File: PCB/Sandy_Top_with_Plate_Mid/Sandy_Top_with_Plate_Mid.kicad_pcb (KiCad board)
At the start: 2 copper layers, 285 x 75.1 mm, 63 parts, among them J1 Conn_02x02_Top_Bottom, J2 Conn_02x02_Top_Bottom, J3 Conn_02x02_Top_Bottom

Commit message: ネジ穴調整、追加
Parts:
- removed D15: D, locallib:D_SOD-123_Emphasized_Direction_Line
- removed EXT_TC7: Conn_01x01, TestPoint:TestPoint_THTPad_D2.0mm_Drill1.0mm
- removed the SW_=1 at (291.3, 27.0)
- added H10: MountingHole, locallib:MountingHole_2.2mm_M2_Pad_minimal, F.Cu at (291.3, 52.0)
- added H11: MountingHole, locallib:MountingHole_2.2mm_M2_Pad_minimal, F.Cu at (138.9, 74.1)
- added H12: MountingHole, locallib:MountingHole_2.2mm_M2_Pad_minimal, F.Cu at (177.0, 74.1)
- added H9: MountingHole, locallib:MountingHole_2.2mm_M2_Pad_minimal, F.Cu at (253.2, 28.2)
- REF**: footprint locallib:60_Outline-Sandy-Top3-with-Mid-plate-from-Mid4 -> locallib:60_Outline-Sandy-DN0040-Top
- moved H6 219.1 mm to (62.7, 28.2), turned to 180 degrees
- moved H5 201.4 mm to (24.6, 52.0)
- moved H4 200.2 mm to (291.3, 20.6), turned to 180 degrees
- moved H3 162.1 mm to (196.1, 20.6), turned to 180 degrees
- moved H1 104.8 mm to (24.6, 20.6)
- moved H2 66.7 mm to (119.9, 20.6)
- moved D9 28.6 mm to (186.6, 30.6)
- moved SW_6 28.6 mm to (186.6, 27.0)
- moved D8 28.6 mm to (167.5, 30.6)
- moved SW_=1 28.6 mm to (167.5, 27.0)
- moved D7 28.6 mm to (148.5, 30.6)
- moved SW_-1 28.6 mm to (148.5, 27.0)
- moved H8 19.1 mm to (196.1, 52.0)
- moved H7 19.0 mm to (119.9, 52.0)
- moved D14 9.53 mm to (281.8, 30.6)
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- renumbered SW_6 to SW_-1, SW_\1 to SW_6, SW_`1 to SW_=1, SW_-1 to SW_INS1
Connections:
- H1 pad 1: Top_GND -> unconnected-(H1-Pad1)
- H2 pad 1: Top_GND -> unconnected-(H2-Pad1)
- H3 pad 1: Top_GND -> unconnected-(H3-Pad1)
- H4 pad 1: Top_GND -> unconnected-(H4-Pad1)
- H5 pad 1: Top_GND -> unconnected-(H5-Pad1)
- H6 pad 1: Top_GND -> unconnected-(H6-Pad1)
- H7 pad 1: Top_GND -> unconnected-(H7-Pad1)
- H8 pad 1: Top_GND -> unconnected-(H8-Pad1)
- J1 pad 4: Top_col7 -> unconnected-(J1-Pin_4-Pad4)_1
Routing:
- net Top_row0: track 286.8 -> 0.00 mm, vias 2 -> 0
- net Top_row5: track 250.6 -> 0.00 mm, vias 2 -> 0
- net Top_col7: track 134.7 -> 0.00 mm, vias 2 -> 0
- net Top_col0: track 125.2 -> 0.00 mm, vias 2 -> 0
- net Top_col6: track 110.4 -> 0.00 mm, vias 2 -> 0
- net Top_col3: track 99.5 -> 0.00 mm, vias 1 -> 0
- net Top_col1: track 91.6 -> 0.00 mm, vias 3 -> 0
- net Top_col2: track 79.6 -> 0.00 mm, vias 5 -> 0
- net Top_col5: track 73.4 -> 0.00 mm, vias 3 -> 0
- net Top_row1: track 66.0 -> 0.00 mm, vias 1 -> 0
- net Top_row6: track 65.9 -> 0.00 mm, vias 1 -> 0
- net Top_col4: track 65.7 -> 0.00 mm, vias 3 -> 0
- net Net-(D3-A): track 10.7 -> 0.00 mm
- net Net-(D8-A): track 10.4 -> 0.00 mm
- net Net-(D7-A): track 10.4 -> 0.00 mm
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- added copper zone on B.Cu, net unconnected-(H5-Pad1)
- added copper zone on F.Cu, net unconnected-(H5-Pad1)
- removed copper zone on B.Cu, net Top_GND
- removed copper zone on F.Cu, net Top_GND
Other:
- outline, holes or cut-outs redrawn
- board text added: "Screw to Bottom ↓"
- board text removed: "SW_6, `, \ の3個の並び順が間違っているが、 v01とのソフト的な互換性を保つため、修正はおこなわない。"

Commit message: 基板間ピン割り当て
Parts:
- moved EXT_TR1 29.9 mm to (119.9, 34.1), turned to 0 degrees
- moved EXT_TR6 26.2 mm to (119.9, 37.7)
- moved EXT_TR5 14.5 mm to (24.6, 34.1)
- moved EXT_TC1 9.53 mm to (81.8, 21.1)
- moved EXT_TC3 9.53 mm to (158.0, 21.1)
- moved EXT_TC5 9.53 mm to (234.2, 21.1)
- moved J2 9.53 mm to (158.0, 29.6)
- moved EXT_TC0 9.52 mm to (43.7, 21.1)
- moved EXT_TC2 9.52 mm to (100.8, 21.1)
- moved EXT_TC4 9.52 mm to (177.0, 21.0)
- moved EXT_TC6 9.52 mm to (272.3, 21.1)
- moved J1 9.52 mm to (177.0, 29.6)
- moved EXT_TR0 4.91 mm to (24.6, 30.6)
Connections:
- H1 pad 1: unconnected-(H1-Pad1) -> Top_col0
- H10 pad 1: unconnected-(H10-Pad1) -> Top_row5
- H11 pad 1: unconnected-(H11-Pad1) -> Top_row1
- H12 pad 1: unconnected-(H12-Pad1) -> Top_row6
- H2 pad 1: unconnected-(H2-Pad1) -> Top_col2
- H3 pad 1: unconnected-(H3-Pad1) -> Top_col4
- H4 pad 1: unconnected-(H4-Pad1) -> Top_col6
- H5 pad 1: unconnected-(H5-Pad1) -> Top_row0
- H6 pad 1: unconnected-(H6-Pad1) -> Top_col1
- H7 pad 1: unconnected-(H7-Pad1) -> Top_col3
- H8 pad 1: unconnected-(H8-Pad1) -> Top_GND
- H9 pad 1: unconnected-(H9-Pad1) -> Top_col5
- J1 pad 4: unconnected-(J1-Pin_4-Pad4)_1 -> Top_GND
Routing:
- net Top_col0: track 0.00 -> 29.2 mm
- added copper zone on B.Cu, net Top_row0
- added copper zone on F.Cu, net Top_row0
- removed copper zone on B.Cu, net unconnected-(H5-Pad1)
- removed copper zone on F.Cu, net unconnected-(H5-Pad1)

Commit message: ネジ穴と接続するピンを調整中
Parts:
- added D15: D, locallib:D_SOD-123_Emphasized_Direction_Line, B.Cu at (148.3, 68.7)
- added D20: D, locallib:D_SOD-123_Emphasized_Direction_Line, B.Cu at (167.5, 68.7)
- added EXT_TR2: Conn_01x01, TestPoint:TestPoint_THTPad_D2.0mm_Drill1.0mm, B.Cu at (142.5, 56.8)
- added H13: MountingHole, locallib:MountingHole_2.2mm_M2_Pad_minimal, F.Cu at (158.0, 74.1)
- added SW_'1: SW_Push, MX_Alps_Hybrid:MXOnly-1U-Hotswap-guide, F.Cu at (167.5, 65.1)
- added SW_;1: SW_Push, MX_Alps_Hybrid:MXOnly-1U-Hotswap-guide, F.Cu at (148.5, 65.1)
- moved H7 30.5 mm to (215.1, 28.2), turned to 180 degrees
- moved H6 30.5 mm to (100.8, 28.2), turned to 180 degrees
- moved H9 29.2 mm to (196.1, 52.0)
- moved H12 29.2 mm to (119.9, 52.0)
- moved EXT_TR1 27.4 mm to (142.5, 49.6)
- moved EXT_TR6 27.4 mm to (142.5, 53.2)
- moved J3 4.38 mm to (136.2, 33.0)
- renumbered H5 to H11, H11 to H12, H6 to H5, H7 to H6, H8 to H7, H9 to H8, H12 to H9
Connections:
- H10 pad 1: Top_row5 -> Top_GND
- H2 pad 1: Top_col2 -> Top_col3
- H6 pad 1: Top_col3 -> Top_col2
- H7 pad 1: Top_GND -> Top_col5
- H8 pad 1: Top_col5 -> Top_row5
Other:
- outline, holes or cut-outs redrawn
- board text added: "#Sandy_kbd DN0040, Top & Plate for Mid by @jpskenn"
- board text removed: "#Sandy_kbd DN0030, Top & Plate for Mid by @jpskenn"

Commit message: ネジ位置調整
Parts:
- SW_-1: footprint MX_Alps_Hybrid:MXOnly-1U-Hotswap-screw-hole-side1-guide -> MX_Alps_Hybrid:MXOnly-1U-Hotswap-screw-hole-side3-guide
- SW_10, SW_2: footprint MX_Alps_Hybrid:MXOnly-1U-Hotswap-guide -> MX_Alps_Hybrid:MXOnly-1U-Hotswap-screw-hole-side3-guide
- SW_4, SW_INS1: footprint MX_Alps_Hybrid:MXOnly-1U-Hotswap-guide -> MX_Alps_Hybrid:MXOnly-1U-Hotswap-screw-hole-side1-guide
- SW_5: footprint MX_Alps_Hybrid:MXOnly-1U-Hotswap-screw-hole-side2-guide -> MX_Alps_Hybrid:MXOnly-1U-Hotswap-guide
- SW_6: footprint MX_Alps_Hybrid:MXOnly-1U-Hotswap-guide -> MX_Alps_Hybrid:MXOnly-1U-Hotswap-screw-hole-side2-guide
- SW_8: footprint MX_Alps_Hybrid:MXOnly-1U-Hotswap-screw-hole-side3-guide -> MX_Alps_Hybrid:MXOnly-1U-Hotswap-guide
- moved H10 5.33 mm to (293.7, 47.2)
- moved H11 5.33 mm to (22.2, 47.2)
- moved EXT_TR1 3.57 mm to (138.9, 49.6)
- moved EXT_TR2 3.57 mm to (138.9, 56.8)
- moved EXT_TR6 3.57 mm to (138.9, 53.2)
- moved H12 1.19 mm to (119.9, 50.8)
- moved H9 1.19 mm to (196.1, 50.8)

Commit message: Top基板のMidプレート部分変更（穴はEdge.Cutじゃない方法で）
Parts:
- REF**: footprint locallib:60_Outline-Sandy-DN0040-Top -> locallib:60_Outline-Sandy-DN0040-Top-sw-hole
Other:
- outline, holes or cut-outs redrawn

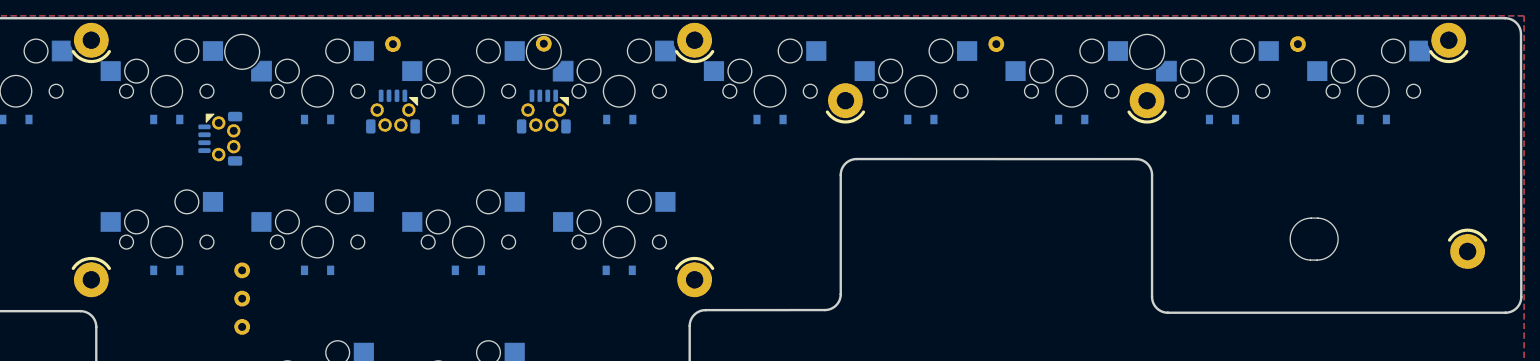
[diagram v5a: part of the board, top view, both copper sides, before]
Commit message: SHコネクタ・ケーブル逃し穴の調整
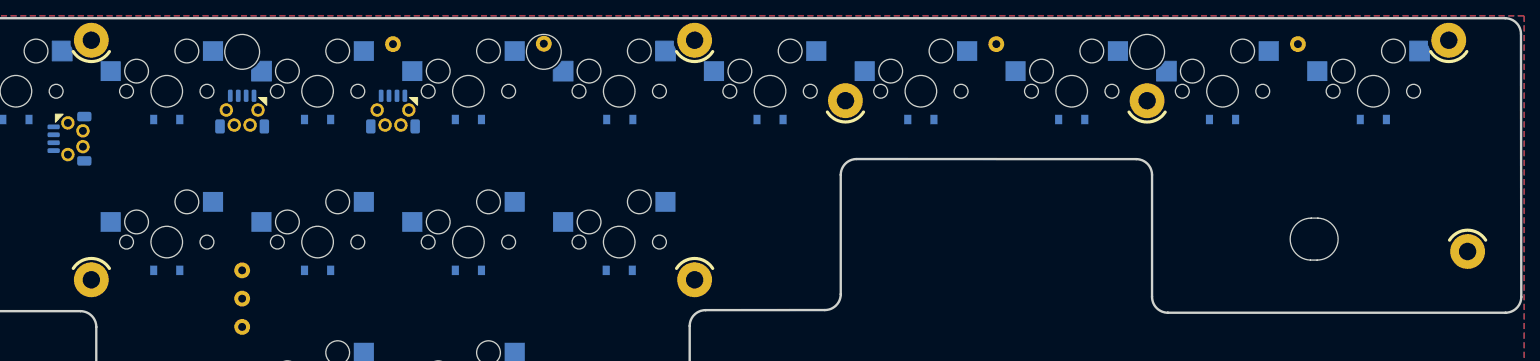
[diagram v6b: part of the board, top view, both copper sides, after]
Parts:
- moved J2 19.1 mm to (138.9, 29.6)
- moved J3 19.0 mm to (117.1, 33.0)
- moved J1 19.0 mm to (158.0, 29.6)
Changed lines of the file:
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@@
 		(allow_soldermask_bridges_in_footprints no)
 		(aux_axis_origin 15.10531 17.478405)
-		(grid_origin 119.88031 52.00653)
+		(grid_origin 136.16781 33.003405)
 		(pcbplotparams
 			(layerselection 0x00310fc_ffffffff)
@@
 		(fp_arc
 			(start 114.175 -9.90004)
-			(mid 114.731476 -11.243582)
+			(mid 114.731482 -11.243546)
 			(end 116.075 -11.80004)
 			(stroke
@@
 		(fp_arc
 			(start 114.923491 -9.898554)
-			(mid 115.274975 -10.747086)
+			(mid 115.274981 -10.74705)
 			(end 116.123491 -11.098554)
 			(stroke
@@
 		(fp_arc
 			(start 116.075 -8.00004)
-			(mid 114.731482 -8.55651)
+			(mid 114.731447 -8.556504)
 			(end 114.175 -9.90004)
 			(stroke
@@
 		(fp_arc
 			(start 116.123491 -8.698554)
-			(mid 115.274982 -9.050056)
+			(mid 115.275017 -9.050062)
 			(end 114.923491 -9.898554)
 			(stroke
@@
 		(fp_arc
 			(start 118.923491 -11.098554)
-			(mid 119.772038 -10.747112)
+			(mid 119.772073 -10.747118)
 			(end 120.123491 -9.898554)
 			(stroke
@@
 		(fp_arc
 			(start 118.975 -11.80004)
-			(mid 120.318488 -11.243516)
+			(mid 120.318452 -11.24351)
 			(end 120.875 -9.90004)
 			(stroke
@@
 		(fp_arc
 			(start 120.123491 -9.898554)
-			(mid 119.772032 -9.050029)
+			(mid 119.772038 -9.049994)
 			(end 118.923491 -8.698554)
 			(stroke
@@
 		(fp_arc
 			(start 120.875 -9.90004)
-			(mid 120.318482 -8.556576)
+			(mid 120.318488 -8.556541)
 			(end 118.975 -8.00004)
 			(stroke
@@
 		(fp_arc
 			(start 27.975 35.345746)
-			(mid 27.389238 36.759982)
+			(mid 27.389238 36.759986)
 			(end 25.975 37.345746)
 			(stroke
@@
 		(fp_arc
 			(start 93.875 -20.001612)
-			(mid 95.289212 -19.41585)
+			(mid 95.289182 -19.41582)
 			(end 95.875 -18.001612)
 			(stroke
@@
 		(fp_arc
 			(start 97.875 -0.60004)
-			(mid 96.460771 -1.1858)
+			(mid 96.460736 -1.185794)
 			(end 95.875 -2.60004)
 			(stroke
@@
 		(fp_arc
 			(start 140.475 -37.80004)
-			(mid 141.889198 -37.214227)
+			(mid 141.889163 -37.214221)
 			(end 142.475 -35.80004)
 			(stroke
@@
 	(footprint "locallib:JST_SH_SM04B-SRSS-TB_1x04-1MP_P1.00mm_Horizontal_wCable_housing_spare_pin"
 		(layer "B.Cu")
-		(at 177.03031 29.57528 180)
+		(at 157.98031 29.57528 180)
 		(descr "JST SH series connector, SM04B-SRSS-TB (http://www.jst-mfg.com/product/pdf/eng/eSH.pdf), generated with kicad-footprint-generator")
 		(tags "connector JST SH top entry")
@@
 	(footprint "locallib:JST_SH_SM04B-SRSS-TB_1x04-1MP_P1.00mm_Horizontal_wCable_housing_spare_pin"
 		(layer "B.Cu")
-		(at 136.16781 33.003405 -90)
+		(at 117.11781 33.003405 -90)
 		(descr "JST SH series connector, SM04B-SRSS-TB (http://www.jst-mfg.com/product/pdf/eng/eSH.pdf), generated with kicad-footprint-generator")
 		(tags "connector JST SH top entry")
@@
 	(footprint "locallib:JST_SH_SM04B-SRSS-TB_1x04-1MP_P1.00mm_Horizontal_wCable_housing_spare_pin"
 		(layer "B.Cu")
-		(at 157.98031 29.57528 180)
+		(at 138.93031 29.57528 180)
 		(descr "JST SH series connector, SM04B-SRSS-TB (http://www.jst-mfg.com/product/pdf/eng/eSH.pdf), generated with kicad-footprint-generator")
 		(tags "connector JST SH top entry")
@@
 	)
 	(gr_text "Top 1"
-		(at 181.79281 31.478405 -90)
+		(at 163.552185 31.478405 -90)
 		(layer "B.SilkS" knockout)
 		(effects
@@
 	)
 	(gr_text "Top 2"
-		(at 162.74281 31.478405 -90)
+		(at 144.502185 31.478405 -90)
 		(layer "B.SilkS" knockout)
 		(effects
@@
 	)
 	(gr_text "Top 3"
-		(at 133.30531 37.878405 0)
+		(at 119.49906 37.878405 0)
 		(layer "B.SilkS" knockout)
 		(effects
@@
 	)
 	(gr_text "to Base"
-		(at 157.98031 35.33778 0)
+		(at 138.93031 35.33778 0)
 		(layer "Eco2.User")
 		(effects
@@
 	)
 	(gr_text "to Base"
-		(at 177.03031 35.33778 0)
+		(at 157.98031 35.33778 0)
 		(layer "Eco2.User")
 		(effects
@@
 	)
 	(gr_text "to Base"
-		(at 142.502185 32.95653 90)
+		(at 123.452185 32.95653 90)
 		(layer "Eco2.User")
 		(effects

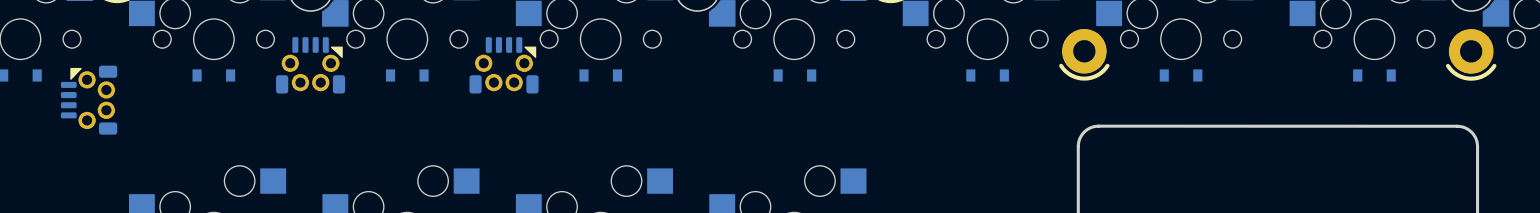
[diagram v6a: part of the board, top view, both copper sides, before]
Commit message: TopのSHコネクタ位置調整。3Dモデル作成
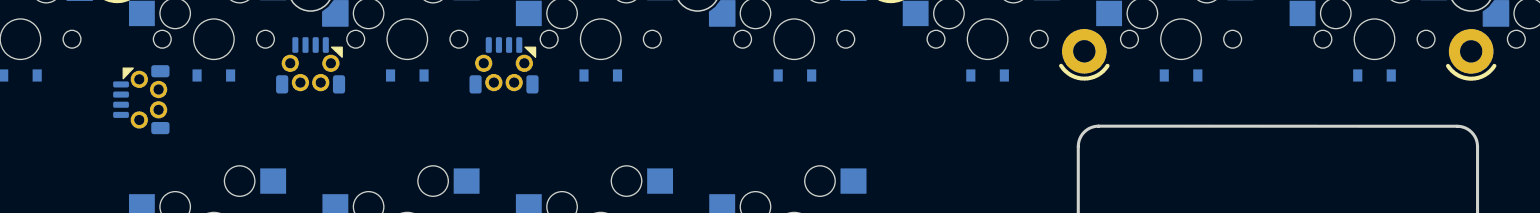
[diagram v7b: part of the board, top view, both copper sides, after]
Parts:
- moved J3 5.14 mm to (122.3, 33.0)
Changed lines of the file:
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@@
 		(allow_soldermask_bridges_in_footprints no)
 		(aux_axis_origin 15.10531 17.478405)
-		(grid_origin 136.16781 33.003405)
+		(grid_origin 15.10531 17.478405)
 		(pcbplotparams
 			(layerselection 0x00310fc_ffffffff)
@@
 		(fp_arc
 			(start 93.875 -20.001612)
-			(mid 95.289182 -19.41582)
+			(mid 95.289189 -19.415797)
 			(end 95.875 -18.001612)
 			(stroke
@@
 	(footprint "locallib:JST_SH_SM04B-SRSS-TB_1x04-1MP_P1.00mm_Horizontal_wCable_housing_spare_pin"
 		(layer "B.Cu")
-		(at 117.11781 33.003405 -90)
+		(at 122.26156 32.95653 -90)
 		(descr "JST SH series connector, SM04B-SRSS-TB (http://www.jst-mfg.com/product/pdf/eng/eSH.pdf), generated with kicad-footprint-generator")
 		(tags "connector JST SH top entry")
@@
 	)
 	(gr_text "Top 3"
-		(at 119.49906 37.878405 0)
+		(at 124.64281 37.83153 0)
 		(layer "B.SilkS" knockout)
 		(effects
@@
 	)
 	(gr_text "to Base"
-		(at 123.452185 32.95653 90)
+		(at 128.595935 32.909655 90)
 		(layer "Eco2.User")
 		(effects

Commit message: ネジ位置調整
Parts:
- moved H10 22.0 mm to (272.3, 52.0)
- moved H11 22.0 mm to (43.7, 52.0)
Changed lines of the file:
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@@
 		(fp_arc
 			(start 114.175 -9.90004)
-			(mid 114.731482 -11.243546)
+			(mid 114.731476 -11.243582)
 			(end 116.075 -11.80004)
 			(stroke
@@
 		(fp_arc
 			(start 114.923491 -9.898554)
-			(mid 115.274981 -10.74705)
+			(mid 115.274975 -10.747086)
 			(end 116.123491 -11.098554)
 			(stroke
@@
 		(fp_arc
 			(start 116.075 -8.00004)
-			(mid 114.731447 -8.556504)
+			(mid 114.731482 -8.55651)
 			(end 114.175 -9.90004)
 			(stroke
@@
 		(fp_arc
 			(start 116.123491 -8.698554)
-			(mid 115.275017 -9.050062)
+			(mid 115.274982 -9.050056)
 			(end 114.923491 -9.898554)
 			(stroke
@@
 		(fp_arc
 			(start 118.923491 -11.098554)
-			(mid 119.772073 -10.747118)
+			(mid 119.772038 -10.747112)
 			(end 120.123491 -9.898554)
 			(stroke
@@
 		(fp_arc
 			(start 118.975 -11.80004)
-			(mid 120.318452 -11.24351)
+			(mid 120.318488 -11.243516)
 			(end 120.875 -9.90004)
 			(stroke
@@
 		(fp_arc
 			(start 120.123491 -9.898554)
-			(mid 119.772038 -9.049994)
+			(mid 119.772032 -9.050029)
 			(end 118.923491 -8.698554)
 			(stroke
@@
 		(fp_arc
 			(start 120.875 -9.90004)
-			(mid 120.318488 -8.556541)
+			(mid 120.318482 -8.556576)
 			(end 118.975 -8.00004)
 			(stroke
@@
 		(fp_arc
 			(start 27.975 35.345746)
-			(mid 27.389238 36.759986)
+			(mid 27.389238 36.759982)
 			(end 25.975 37.345746)
 			(stroke
@@
 		(fp_arc
 			(start 97.875 -0.60004)
-			(mid 96.460736 -1.185794)
+			(mid 96.460771 -1.1858)
 			(end 95.875 -2.60004)
 			(stroke
@@
 		(fp_arc
 			(start 140.475 -37.80004)
-			(mid 141.889163 -37.214221)
+			(mid 141.889198 -37.214227)
 			(end 142.475 -35.80004)
 			(stroke
@@
 	(footprint "locallib:MountingHole_2.2mm_M2_Pad_minimal"
 		(layer "F.Cu")
-		(at 22.24906 47.24403)
+		(at 43.68031 52.00653)
 		(descr "Mounting Hole 2.2mm, M2")
 		(tags "mounting hole 2.2mm m2")
@@
 	(footprint "locallib:MountingHole_2.2mm_M2_Pad_minimal"
 		(layer "F.Cu")
-		(at 293.71156 47.24403)
+		(at 272.28031 52.00653)
 		(descr "Mounting Hole 2.2mm, M2")
 		(tags "mounting hole 2.2mm m2")
